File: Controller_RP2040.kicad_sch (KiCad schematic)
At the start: 9 parts, among them J2 Conn_ARM_SWD_TagConnect_TC203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, U3 NCP1117-3.3_SOT223

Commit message: Annotation update
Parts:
- renumbered D1 to D5, D2 to D6, R15 to R5
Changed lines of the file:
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@@
 		(on_board yes)
 		(dnp no)
-		(property "Reference" "R15"
+		(property "Reference" "R5"
 			(at 271.145 30.988 0)
 			(effects
@@
 			(project "Mad_RP2040"
 				(path "/eedae293-eb5b-47bd-b383-bccfdf81bf72/4e3cb99d-3a42-46ca-abb7-444fcb451820"
-					(reference "R15")
+					(reference "R5")
 					(unit 1)
 				)
@@
 		(on_board yes)
 		(dnp no)
-		(property "Reference" "D2"
+		(property "Reference" "D6"
 			(at 271.78 38.735 90)
 			(effects
@@
 			(project "Mad_RP2040"
 				(path "/eedae293-eb5b-47bd-b383-bccfdf81bf72/4e3cb99d-3a42-46ca-abb7-444fcb451820"
-					(reference "D2")
+					(reference "D6")
 					(unit 1)
 				)
@@
 		(on_board yes)
 		(dnp no)
-		(property "Reference" "#PWR06"
+		(property "Reference" "#PWR011"
 			(at 199.39 88.265 0)
 			(effects
@@
 			(project "Mad_RP2040"
 				(path "/eedae293-eb5b-47bd-b383-bccfdf81bf72/4e3cb99d-3a42-46ca-abb7-444fcb451820"
-					(reference "#PWR06")
+					(reference "#PWR011")
 					(unit 1)
 				)
@@
 		(on_board yes)
 		(dnp no)
-		(property "Reference" "D1"
+		(property "Reference" "D5"
 			(at 231.775 28.575 0)
 			(effects
@@
 			(project "Mad_RP2040"
 				(path "/eedae293-eb5b-47bd-b383-bccfdf81bf72/4e3cb99d-3a42-46ca-abb7-444fcb451820"
-					(reference "D1")
+					(reference "D5")
 					(unit 1)
 				)

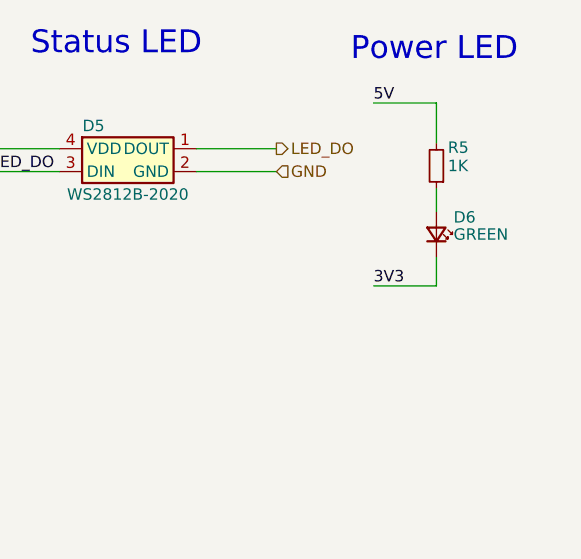
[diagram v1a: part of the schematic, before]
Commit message: Update github actions
Remove double up on actions

Remove kibot config file to what the action is looking for

Update date on title block

Update github actions

update github action

update schematic

Add options.yaml
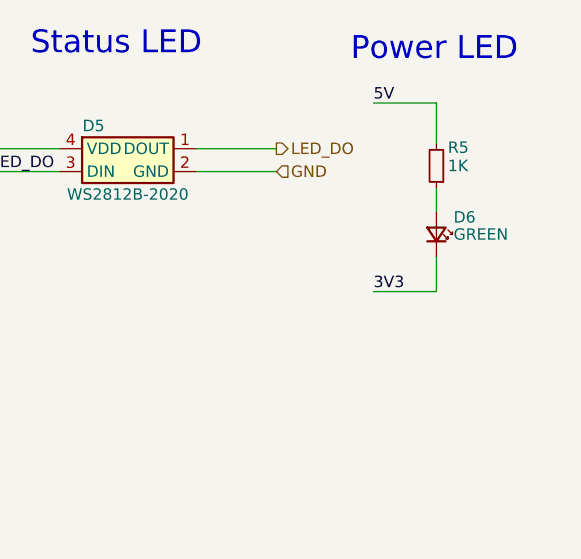
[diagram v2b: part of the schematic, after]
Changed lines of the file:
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@@
 	(wire
 		(pts
-			(xy 262.89 46.355) (xy 269.875 46.355)
+			(xy 262.89 46.99) (xy 269.875 46.99)
 		)
 		(stroke
@@
 	(wire
 		(pts
-			(xy 269.875 43.18) (xy 269.875 46.355)
+			(xy 269.875 43.18) (xy 269.875 46.99)
 		)
 		(stroke
@@
 	)
 	(label "3V3"
-		(at 262.89 46.355 0)
-		(fields_autoplaced yes)
-		(effects
+		(at 262.89 46.99 0)
+		(fields_autoplaced yes)
+		(effects

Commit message: Finish off part placement
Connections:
- net VBUS is gone; now on net 5V: R3.1
- net 3V3: no longer D6.1 (K)
- net GND: now also D6.1 (K)
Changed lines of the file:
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@@
+	(wire
+		(pts
+			(xy 193.675 84.455) (xy 199.39 84.455)
+		)
+		(stroke
+			(width 0)
+			(type default)
+		)
+	)
 	(wire
 		(pts
@@
 		)
 	)
+	(label "5V"
+		(at 193.675 84.455 0)
+		(fields_autoplaced yes)
+		(effects
+			(font
+				(size 1.27 1.27)
+			)
+			(justify left bottom)
+		)
+	)
 	(label "SWCLK"
 		(at 108.585 84.455 0)
@@
 		)
 	)
-	(label "3V3"
+	(label "GND"
 		(at 262.89 46.99 0)
 		(fields_autoplaced yes)
@@
 					(unit 1)
 				)
-			)
-		)
-	)
-	(symbol
-		(lib_id "power:VBUS")
-		(at 199.39 84.455 0)
-		(unit 1)
-		(exclude_from_sim no)
-		(in_bom yes)
-		(on_board yes)
-		(dnp no)
-		(property "Reference" "#PWR011"
-			(at 199.39 88.265 0)
-			(effects
-				(font
-					(size 1.27 1.27)
-				)
-				(hide yes)
-			)
-		)
-		(property "Value" "VBUS"
-			(at 199.39 80.01 0)
-			(effects
-				(font
-					(size 1.27 1.27)
-				)
-			)
-		)
-		(property "Footprint" ""
-			(at 199.39 84.455 0)
-			(effects
-				(font
-					(size 1.27 1.27)
-				)
-				(hide yes)
-			)
-		)
-		(property "Datasheet" ""
-			(at 199.39 84.455 0)
-			(effects
-				(font
-					(size 1.27 1.27)
-				)
-				(hide yes)
-			)
-		)
-		(property "Description" "Power symbol creates a global label with name \"VBUS\""
-			(at 199.39 84.455 0)
-			(effects
-				(font
-					(size 1.27 1.27)
-				)
-				(hide yes)
-			)
-		)
-		(pin "1"
-		)
-		(instances
-			(project "Mad_RP2040"
-				(path "/eedae293-eb5b-47bd-b383-bccfdf81bf72/4e3cb99d-3a42-46ca-abb7-444fcb451820"
-					(reference "#PWR011")
-					(unit 1)
-				)

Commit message: Cleanup bom, remove spaces and lcsc fields
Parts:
- D5: MPN WS2812B-2020 -> WS2812B-2020; MPN  WS2812C-2020 -> (none); Manufacturer Worldsemi -> Worldsemi
- R3, R4, R5: Price $0.16 -> $0.16

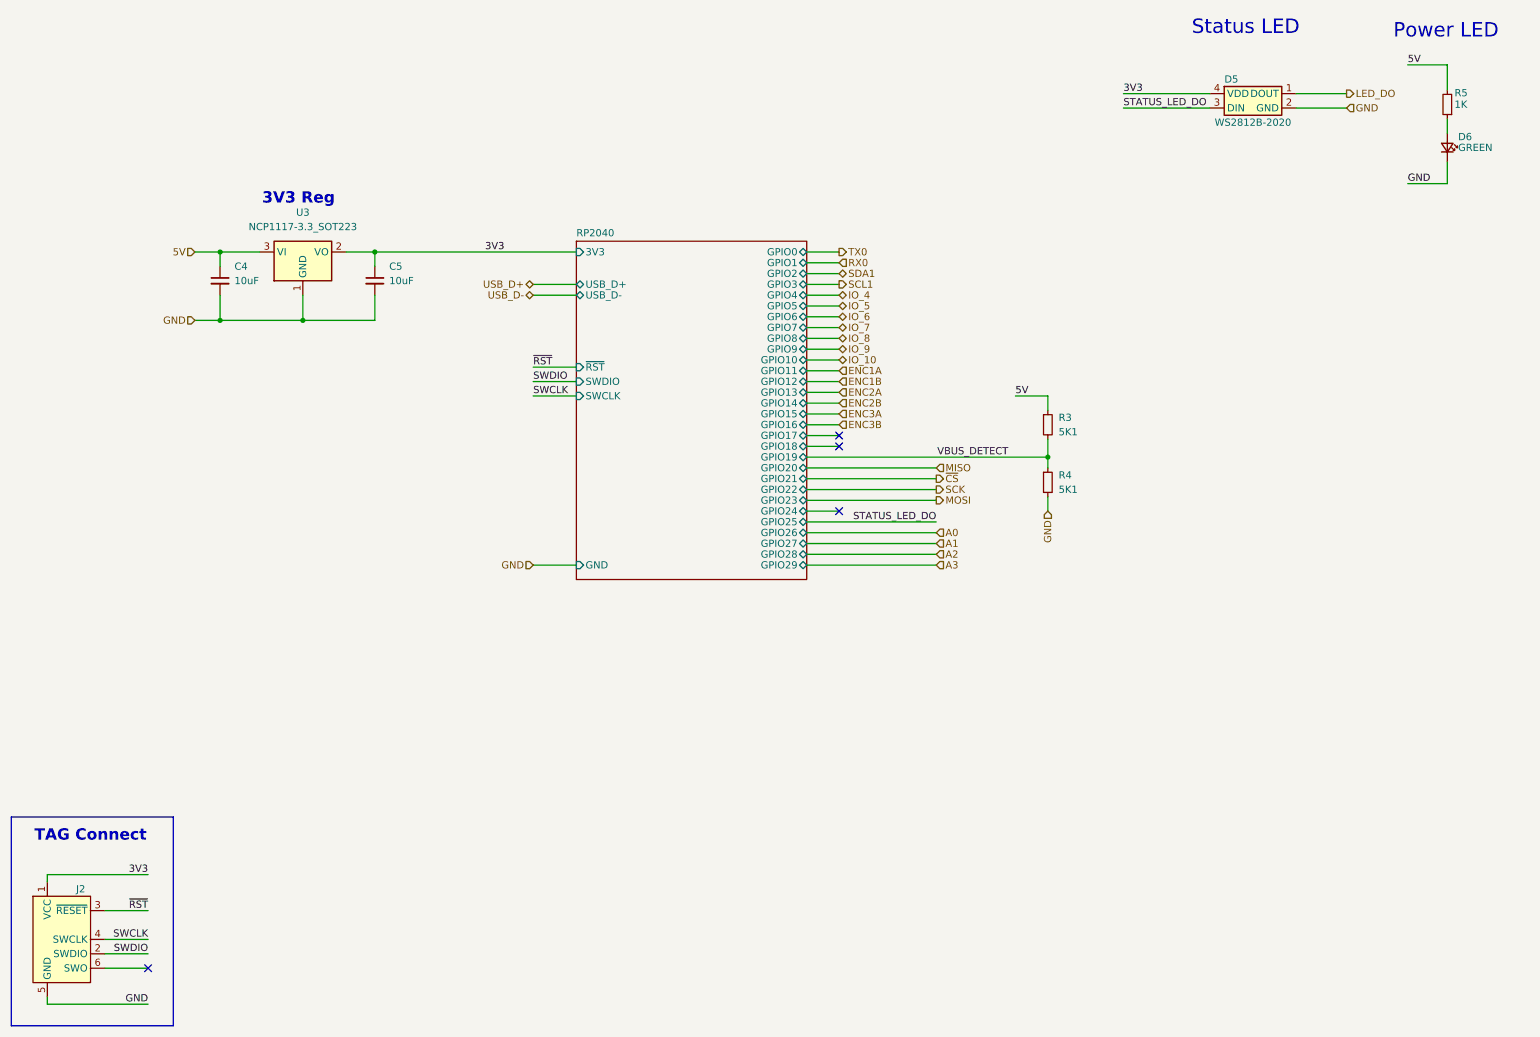
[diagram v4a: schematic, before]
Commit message: Update Models, Finalize LED selections, add backlight, ...
 add mounting holes, add fids, cleanup
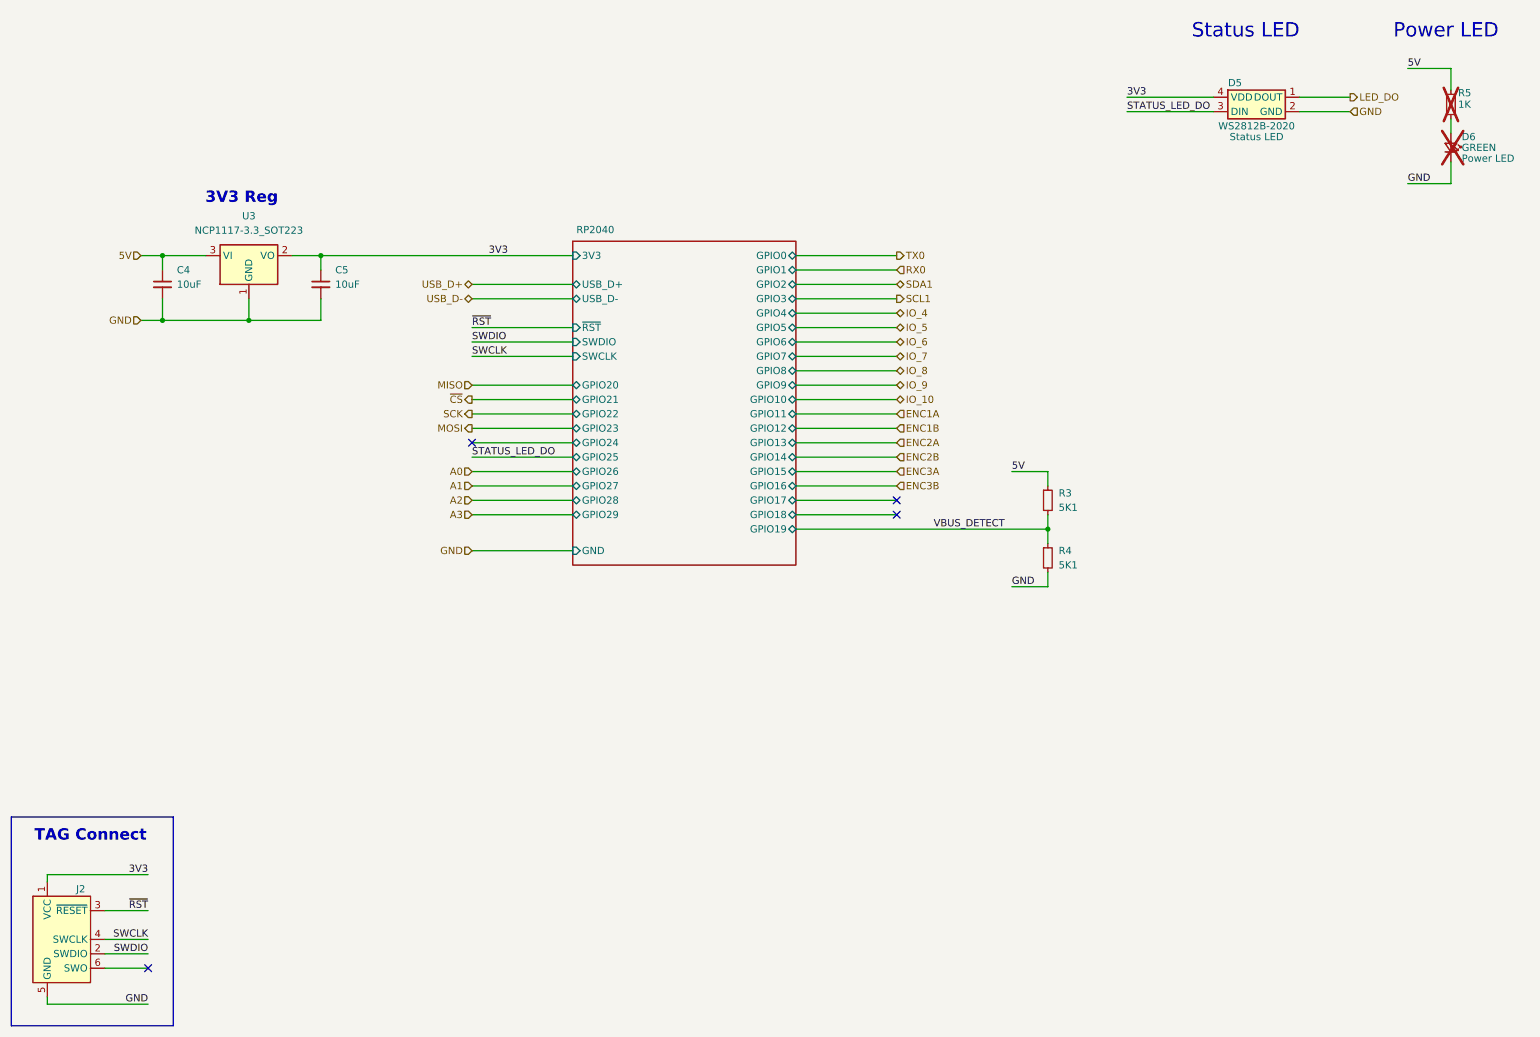
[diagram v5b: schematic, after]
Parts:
- D5: Interface (none) -> Status LED; Rating 3.7...5.3V -> 3.7-5.3V
- D6: Interface (none) -> Power LED; now not fitted
- R5: now not fitted
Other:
- company: MadMan -> ${COMPANY}
- title: RP2040 -> ${TITLE}
- moved on the sheet: C4, C5, D5, R3, R4, U3

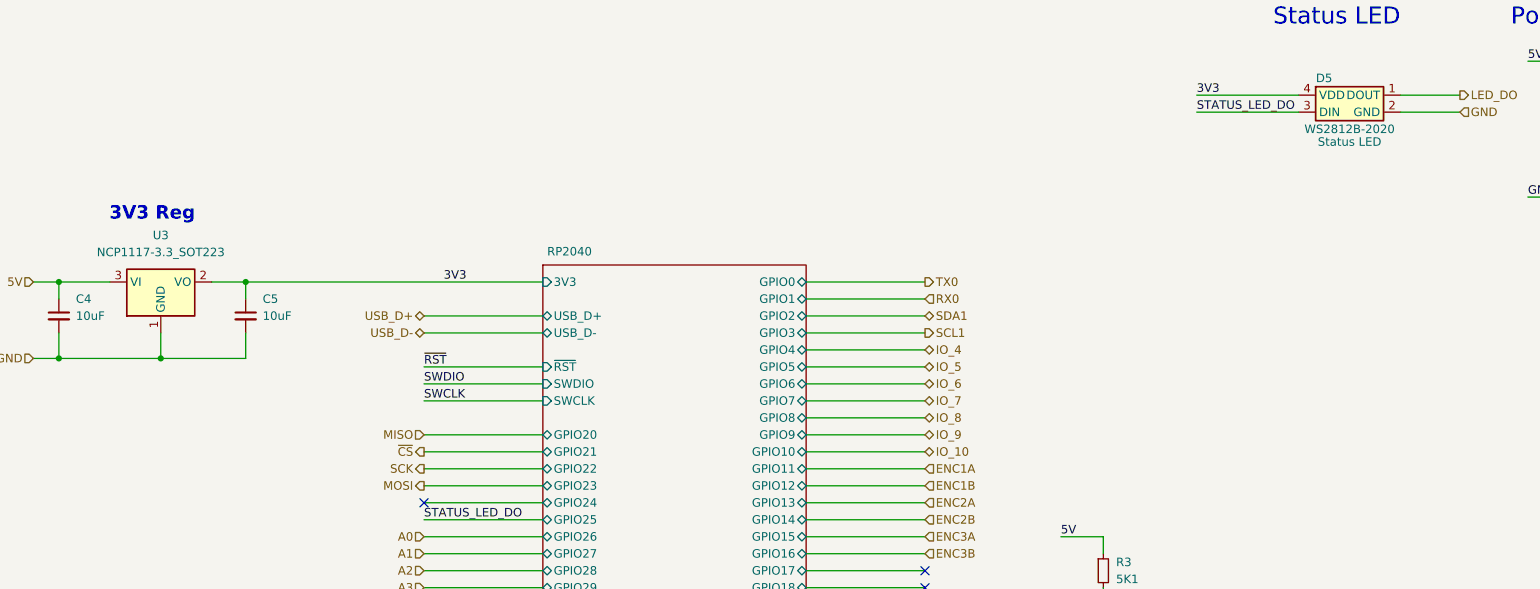
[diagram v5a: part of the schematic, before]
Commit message: BOM update, add lcsc pn to  componenets.
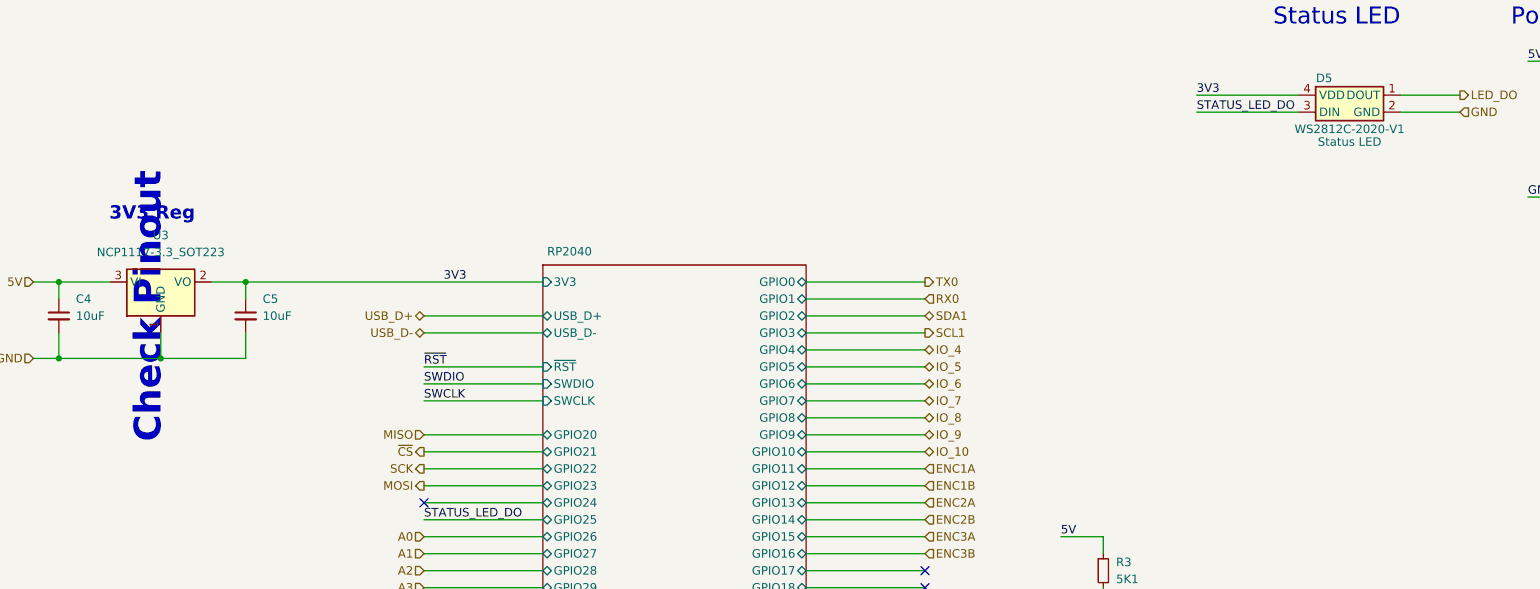
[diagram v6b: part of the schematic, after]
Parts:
- D5: value WS2812B-2020 -> WS2812C-2020-V1; LCSC PN (none) -> C2976072; MPN WS2812B-2020 -> WS2812C-2020-V1; Supplier PN C965555 -> C2976072
- D6: LCSC PN (none) -> C6848499
- R3, R4: LCSC PN (none) -> C105872
- R5: LCSC PN (none) -> C106235
- U3: LCSC PN (none) -> C233236
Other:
- note added: "Check Pinout"
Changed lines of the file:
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@@
+		)
+	)
+	(text "Check Pinout"
+		(exclude_from_sim no)
+		(at 56.515 63.5 90)
+		(effects
+			(font
+				(size 4 4)
+				(thickness 0.8)
+				(bold yes)
+			)
 		)
 	)
@@
 			)
 		)
+		(property "LCSC PN" "C6848499"
+			(at 270.51 40.64 0)
+			(effects
+				(font
+					(size 1.27 1.27)
+				)
+				(hide yes)
+			)
+		)
 		(pin "1"
 		)
@@
 		)
 		(property "Substitute" ""
+			(at 58.42 59.69 0)
+			(effects
+				(font
+					(size 1.27 1.27)
+				)
+				(hide yes)
+			)
+		)
+		(property "LCSC PN" "C233236"
 			(at 58.42 59.69 0)
 			(effects
@@
 			)
 		)
+		(property "Price" ""
+			(at 25.4 180.34 0)
+			(effects
+				(font
+					(size 1.27 1.27)
+				)
+				(hide yes)
+			)
+		)
+		(property "Interface" ""
+			(at 25.4 180.34 0)
+			(effects
+				(font
+					(size 1.27 1.27)
+				)
+				(hide yes)
+			)
+		)
+		(property "Rating" ""
+			(at 25.4 180.34 0)
+			(effects
+				(font
+					(size 1.27 1.27)
+				)
+				(hide yes)
+			)
+		)
+		(property "Supplier" ""
+			(at 25.4 180.34 0)
+			(effects
+				(font
+					(size 1.27 1.27)
+				)
+				(hide yes)
+			)
+		)
+		(property "Supplier PN" ""
+			(at 25.4 180.34 0)
+			(effects
+				(font
+					(size 1.27 1.27)
+				)
+				(hide yes)
+			)
+		)
+		(property "Manufacturer" ""
+			(at 25.4 180.34 0)
+			(effects
+				(font
+					(size 1.27 1.27)
+				)
+				(hide yes)
+			)
+		)
+		(property "MPN" ""
+			(at 25.4 180.34 0)
+			(effects
+				(font
+					(size 1.27 1.27)
+				)
+				(hide yes)
+			)
+		)
 		(pin "1"
 		)
@@
 			)
 		)
+		(property "LCSC PN" "C106235"
+			(at 270.51 33.02 0)
+			(effects
+				(font
+					(size 1.27 1.27)
+				)
+				(hide yes)
+			)
+		)
 		(pin "1"
 		)
@@
 		)
 		(property "Substitute" ""
+			(at 199.39 113.03 0)
+			(effects
+				(font
+					(size 1.27 1.27)
+				)
+				(hide yes)
+			)
+		)
+		(property "LCSC PN" "C105872"
 			(at 199.39 113.03 0)
 			(effects
@@
 			)
 		)
-		(property "Value" "WS2812B-2020"
+		(property "Value" "WS2812C-2020-V1"
 			(at 236.22 36.83 0)
 			(effects
@@
 			)
 		)
-		(property "Supplier PN" "C965555"
+		(property "Supplier PN" "C2976072"
 			(at 236.22 33.02 0)
 			(effects
@@
 			)
 		)
-		(property "MPN" "WS2812B-2020"
+		(property "MPN" "WS2812C-2020-V1"
 			(at 236.22 33.02 0)
 			(effects
@@
 		)
 		(property "Substitute" ""
+			(at 236.22 33.02 0)
+			(effects
+				(font
+					(size 1.27 1.27)
+				)
+				(hide yes)
+			)
+		)
+		(property "LCSC PN" "C2976072"
 			(at 236.22 33.02 0)
 			(effects
@@
 			(at 199.39 102.87 0)
 			(effects
+				(font
+					(size 1.27 1.27)
+				)
+				(hide yes)
+			)
+		)
+		(property "LCSC PN" "C105872"
+			(at 199.39 102.87 0)
+			(effects

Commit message: BOM update
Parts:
- C4, C5: LCSC PN (none) -> C472857
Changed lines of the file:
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@@
+			)
+		)
+		(property "LCSC PN" "C472857"
+			(at 43.18 64.77 0)
+			(effects
+				(font
+					(size 1.27 1.27)
+				)
+				(hide yes)
 			)
 		)
@@
 			(at 71.12 64.77 0)
 			(effects
+				(font
+					(size 1.27 1.27)
+				)
+				(hide yes)
+			)
+		)
+		(property "LCSC PN" "C472857"
+			(at 71.12 64.77 0)
+			(effects

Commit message: BOM consolidation
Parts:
- added R13, R14: 27R, Resistor_SMD:R_0402_1005Metric, symbol Device:R_Small
- C4, C5: LCSC PN C472857 -> C2932476
- U3: value NCP1117-3.3_SOT223 -> NCP1117-3.3
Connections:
- net USB_D+: now also R13.1
- net USB_D-: now also R14.1
- new net RP2040/USB_D+: R13.2
- new net RP2040/USB_D-: R14.2
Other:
- note removed: "Check Pinout"
